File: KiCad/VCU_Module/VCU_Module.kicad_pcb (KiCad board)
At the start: 4 copper layers, 85.1 x 64.6 mm, 44 parts, among them IC1 STM32C092RCT6, J1 5810132011, J11 Conn_ST_STDC14, J5 pin header, J7 5V, J8 3V3, J9 GND, Q1 AO3401A, SW2 SW_Push, U1 OKI-78SR-5_1.5-W36-C, U2 TLV75533PDBV, U6 MCP2562FDT-H_SN

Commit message: added peripherals to mcu
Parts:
- moved CR1 104.9 mm to (134.0, 92.0)
- moved C13 104.9 mm to (91.3, 82.1)
- moved C14 104.9 mm to (91.3, 85.1)
- moved C15 104.9 mm to (91.3, 88.1)
- moved C16 104.9 mm to (91.3, 91.1)
- moved C17 104.9 mm to (91.3, 94.1)
- moved D3 104.9 mm to (96.0, 107.5)
- moved J5 104.9 mm to (121.0, 108.2)
- moved J7 104.9 mm to (125.5, 108.2)
- moved J9 104.9 mm to (116.4, 108.2)
- moved Q1 104.9 mm to (120.1, 101.6)
- moved SW2 104.9 mm to (101.0, 97.1)
- moved TP12 104.9 mm to (87.3, 82.3)
- moved TP13 104.9 mm to (87.3, 85.9)
- moved TP14 104.9 mm to (87.3, 89.4)
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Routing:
- added copper zone on B.Cu, net (none)
- added copper zone on F.Cu, net (none)

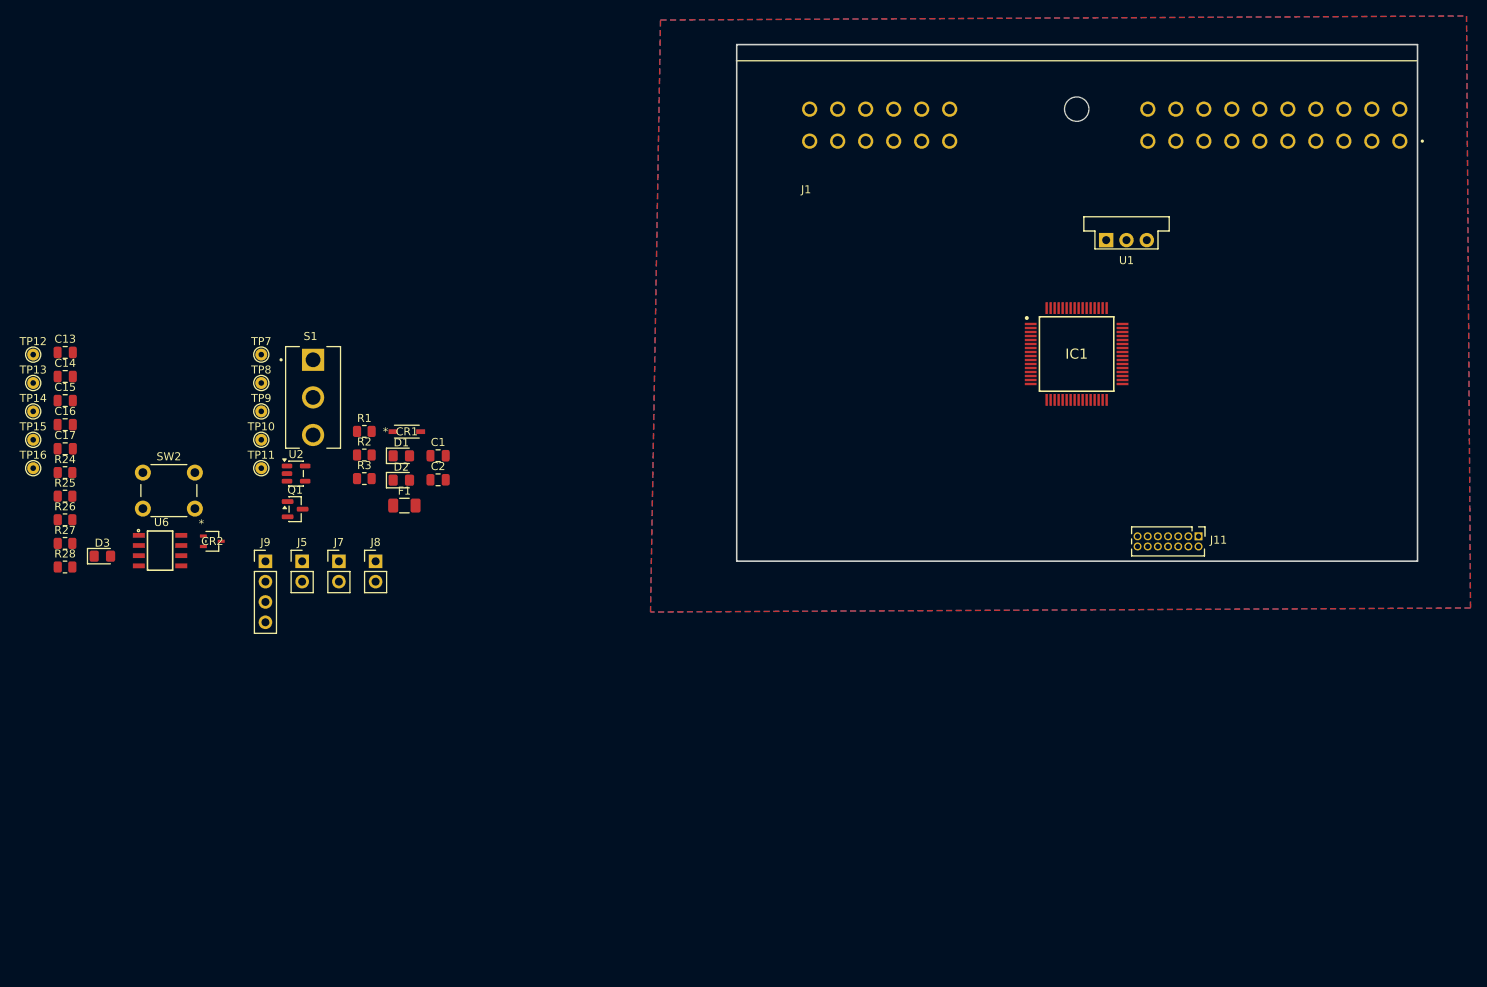
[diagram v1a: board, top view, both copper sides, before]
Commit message: added peripheral pins with the most functionality based on stm32c092rc datasheet, started placing components and routing traces on pcb
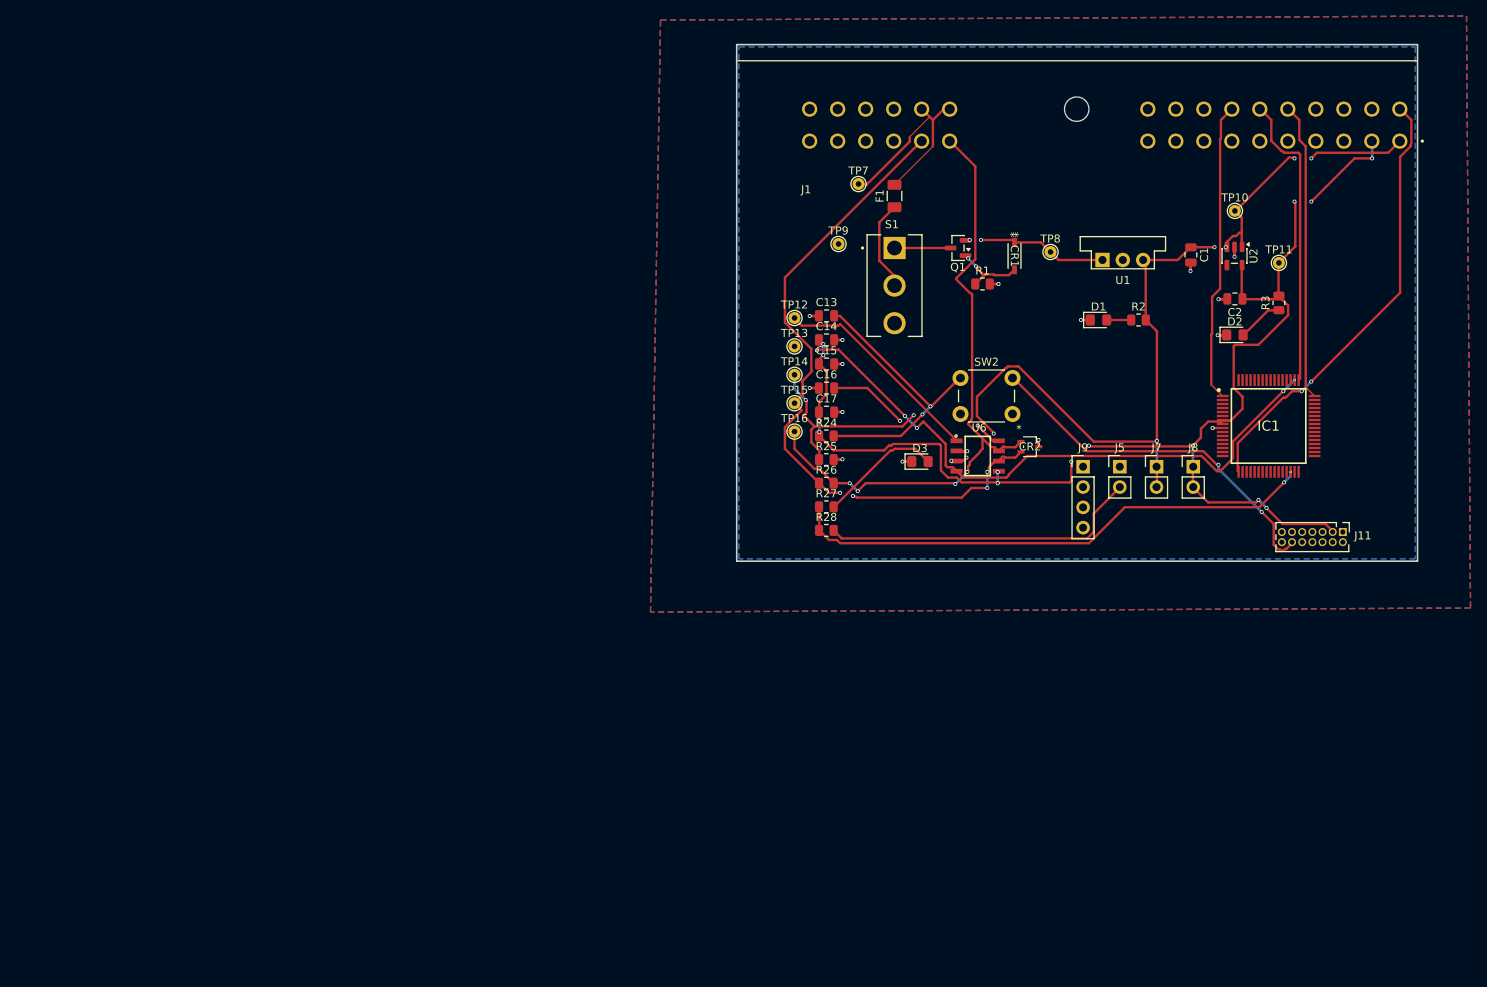
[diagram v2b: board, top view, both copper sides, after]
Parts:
- moved TP11 129.8 mm to (243.1, 70.9)
- moved TP10 125.0 mm to (237.6, 64.4)
- moved U2 120.4 mm to (237.5, 70.0), turned to -90 degrees
- moved R3 116.4 mm to (243.1, 75.9), turned to 90 degrees
- moved D2 105.8 mm to (237.6, 79.9)
- moved CR2 102.9 mm to (211.9, 93.8)
- moved J8 102.9 mm to (232.3, 96.3)
- moved U6 102.9 mm to (205.4, 95.0)
- moved D3 102.9 mm to (198.2, 95.7)
- moved J5 102.9 mm to (223.2, 96.3)
- moved J7 102.9 mm to (227.8, 96.3)
- moved J9 102.9 mm to (218.6, 96.3)
- moved SW2 102.9 mm to (203.2, 85.2)
- moved C2 102.1 mm to (237.6, 75.4), turned to 180 degrees
- moved TP8 100.0 mm to (214.5, 69.5)
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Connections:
- CR2 pad 1: /CANH -> /MCU/CANH
- CR2 pad 2: /CANL -> /MCU/CANL
- IC1 pad 1: unconnected-(IC1-PC11-Pad1) -> /A17
- IC1 pad 13: /MCU/SHUTDOWN -> unconnected-(IC1-PC0-Pad13)
- IC1 pad 14: /MCU/GPIO_SPARE1 -> unconnected-(IC1-PC1-Pad14)
- IC1 pad 15: /MCU/GPIO_SPARE2 -> unconnected-(IC1-PC2-Pad15)
- IC1 pad 16: /MCU/GPIO_SPARE3 -> unconnected-(IC1-PC3-Pad16)
- IC1 pad 17: unconnected-(IC1-PA0-Pad17) -> /A11
- IC1 pad 18: unconnected-(IC1-PA1-Pad18) -> /A12
- IC1 pad 21: unconnected-(IC1-PA4-Pad21) -> /A13
- IC1 pad 22: unconnected-(IC1-PA5-Pad22) -> /A8
- IC1 pad 23: unconnected-(IC1-PA6-Pad23) -> /A5
- IC1 pad 24: unconnected-(IC1-PA7-Pad24) -> /A6
- IC1 pad 25: unconnected-(IC1-PC4-Pad25) -> /A19
- IC1 pad 26: unconnected-(IC1-PC5-Pad26) -> /A20
- IC1 pad 3: unconnected-(IC1-PC13-Pad3) -> /A18
- IC1 pad 36: unconnected-(IC1-PA8-Pad36) -> /A14
- IC1 pad 37: unconnected-(IC1-PA9-Pad37) -> /A3
- IC1 pad 42: unconnected-(IC1-PA10-Pad42) -> /A4
- IC1 pad 47: unconnected-(IC1-PA15-Pad47) -> /A7
- IC1 pad 48: unconnected-(IC1-PC8-Pad48) -> /A15
- IC1 pad 49: unconnected-(IC1-PC9-Pad49) -> /A16
- IC1 pad 57: unconnected-(IC1-PB3-Pad57) -> /MCU/PB3
- IC1 pad 60: unconnected-(IC1-PB6-Pad60) -> /MCU/GPIO_SPARE1_PB6
- IC1 pad 61: unconnected-(IC1-PB7-Pad61) -> /MCU/GPIO_SPARE2_PB7
- IC1 pad 62: unconnected-(IC1-PB8-Pad62) -> /MCU/GPIO_SPARE3_PB8
- IC1 pad 63: unconnected-(IC1-PB9-Pad63) -> /MCU/GPIO_SPARE4_PB9
- J1 pad A1: +12V -> +5V
- J1 pad A11: unconnected-(J1-PadA11) -> /A11
- J1 pad A12: unconnected-(J1-PadA12) -> /A12
- J1 pad A13: unconnected-(J1-PadA13) -> /A13
- J1 pad A14: unconnected-(J1-PadA14) -> /A14
- J1 pad A15: unconnected-(J1-PadA15) -> /A15
- J1 pad A16: unconnected-(J1-PadA16) -> /A16
- J1 pad A17: unconnected-(J1-PadA17) -> /A17
- J1 pad A18: /CANH -> /A18
- J1 pad A19: /CANL -> /A19
- J1 pad A2: +12V -> +3V3
- J1 pad A20: GND -> /A20
- J1 pad A3: unconnected-(J1-PadA3) -> /A3
- J1 pad A4: unconnected-(J1-PadA4) -> /A4
- J1 pad A5: unconnected-(J1-PadA5) -> /A5
- J1 pad A6: unconnected-(J1-PadA6) -> /A6
- J1 pad A7: unconnected-(J1-PadA7) -> /A7
- J1 pad A8: unconnected-(J1-PadA8) -> /A8
- J1 pad B1: +5V -> /MCU/CANH
- J1 pad B10: /MCU/SHUTDOWN -> unconnected-(J1-PadB10)
- J1 pad B11: unconnected-(J1-PadB11) -> GND
- J1 pad B2: +5V -> /MCU/CANL
- J1 pad B3: +5V -> /MCU/GPIO_SPARE1_PB6
- J1 pad B4: GND -> /MCU/GPIO_SPARE2_PB7
- J1 pad B5: GND -> /MCU/GPIO_SPARE4_PB9
- J1 pad B6: GND -> /MCU/GPIO_SPARE3_PB8
- J1 pad B7: /MCU/GPIO_SPARE1 -> +12V
- J1 pad B8: /MCU/GPIO_SPARE2 -> +12V
- J1 pad B9: /MCU/GPIO_SPARE3 -> unconnected-(J1-PadB9)
- J11 pad 8: unconnected-(J11-JTDO/SWO-Pad8) -> /MCU/PB3
- R26 pad 1: /CANL -> /MCU/CANL
- R26 pad 2: /CANH -> /MCU/CANH
- TP15 pad 1: /CANL -> /MCU/CANL
- TP16 pad 1: /CANH -> /MCU/CANH
- U6 pad 6: /CANL -> /MCU/CANL
- U6 pad 7: /CANH -> /MCU/CANH
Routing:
- net +3V3: track 0.00 -> 160.4 mm, vias 0 -> 14
- net +5V: track 0.00 -> 131.1 mm, vias 0 -> 9
- net Net-(IC1-PF2-NRST): track 0.00 -> 88.7 mm, vias 0 -> 4
- net /MCU/CANL: track 0.00 -> 84.9 mm, vias 0 -> 4
- net /MCU/CAN_RXD: track 0.00 -> 79.6 mm, vias 0 -> 5
- net /MCU/CANH: track 0.00 -> 79.0 mm, vias 0 -> 4
- net Net-(IC1-PB10): track 0.00 -> 66.5 mm, vias 0 -> 2
- net /A11: track 0.00 -> 55.7 mm, vias 0 -> 2
- net /MCU/FAULT_LED: track 0.00 -> 40.2 mm
- net /MCU/STDBY: track 0.00 -> 37.6 mm, vias 0 -> 3
- net /A17: track 0.00 -> 37.6 mm
- net /A15: track 0.00 -> 37.3 mm
- net /A16: track 0.00 -> 36.9 mm
- net +12V: track 0.00 -> 27.5 mm
- net /MCU/CAN_TXD: track 0.00 -> 26.9 mm
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- added copper zone on B.Cu, net GND

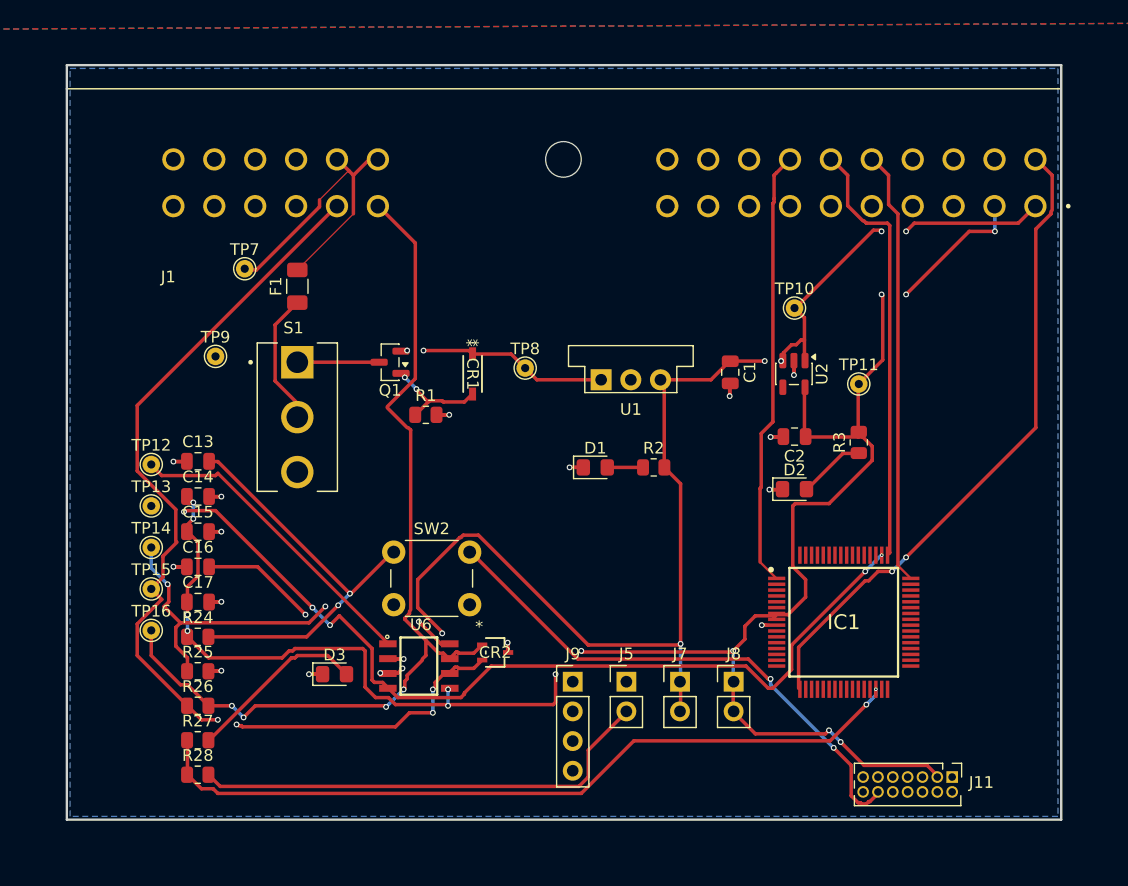
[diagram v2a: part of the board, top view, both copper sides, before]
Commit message: placed pcb components, ran traces, still need to fix erc errors
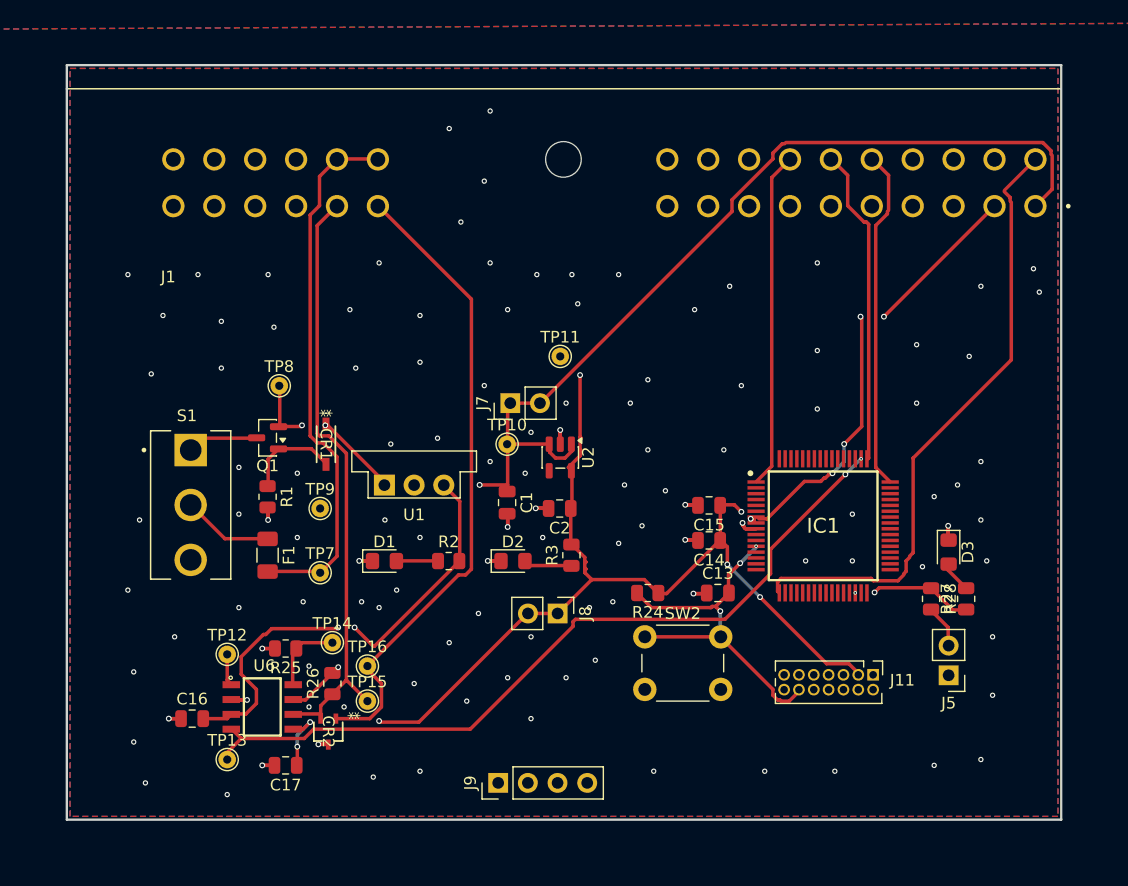
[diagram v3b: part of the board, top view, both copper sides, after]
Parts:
- moved R27 66.9 mm to (252.2, 89.2), turned to 90 degrees
- moved R28 64.5 mm to (249.2, 89.2), turned to -90 degrees
- moved D3 53.6 mm to (250.7, 85.2), turned to -90 degrees
- moved C13 45.9 mm to (231.0, 88.8)
- moved C14 43.9 mm to (230.2, 84.2), turned to 180 degrees
- moved C15 43.8 mm to (230.2, 81.2), turned to 180 degrees
- moved R24 38.7 mm to (225.0, 88.8), turned to 180 degrees
- moved J7 27.9 mm to (213.2, 72.5), turned to 90 degrees
- moved J5 27.6 mm to (250.7, 95.8), turned to 180 degrees
- moved TP10 27.2 mm to (213.0, 76.0)
- moved TP7 26.8 mm to (197.0, 87.0)
- moved R3 26.4 mm to (218.5, 85.5)
- moved TP11 25.7 mm to (217.5, 68.5)
- moved D2 24.9 mm to (213.5, 86.0)
- moved F1 23.2 mm to (192.5, 85.5), turned to -90 degrees
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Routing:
- net Net-(IC1-PB10): track 66.5 -> 10.5 mm
- net Net-(IC1-PF2-NRST): track 88.7 -> 32.8 mm, vias 4 -> 3
- net /MCU/FAULT_LED: track 40.2 -> 3.68 mm
- net /MCU/CANL: track 84.9 -> 52.1 mm, vias 4 -> 0
- net /MCU/STDBY: track 37.6 -> 6.61 mm, vias 3 -> 0
- net +3V3: track 160.4 -> 133.0 mm, vias 14 -> 12
- net /MCU/CAN_TXD: track 26.9 -> 2.82 mm
- net +12V: track 27.5 -> 46.1 mm
- net /MCU/CANH: track 79.0 -> 62.3 mm, vias 4 -> 1
- net Net-(D3-A): track 15.5 -> 2.72 mm
- net /MCU/CAN_RXD: track 79.6 -> 67.8 mm, vias 5 -> 2
- net /A16: track 36.9 -> 27.2 mm
- net +5V: track 131.1 -> 122.3 mm, vias 9 -> 3
- net /A17: track 37.6 -> 28.9 mm
- net /A15: track 37.3 -> 29.1 mm
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- added copper zone on F.Cu, net GND
